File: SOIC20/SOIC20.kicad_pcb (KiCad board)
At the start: 2 copper layers, 25.7 x 18 mm, 7 parts, among them J1 Conn_01x10, J2 Conn_02x10_Counter_Clockwise, J4 Conn_02x10_Counter_Clockwise, J5 Conn_01x10

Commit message: Board Updates
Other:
- board size 25.7 x 18 mm -> 25.4 x 17.8 mm
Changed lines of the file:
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@@
       (xy -0.06096 3.169456) (xy -0.06096 2.6924) (xy 0.07112 2.6924) (xy 0.07112 2.926926)) (layer F.SilkS) (width 0.01))
   )
+  (gr_line (start 77.089 43.7896) (end 77.089 28.5496) (layer Edge.Cuts) (width 0.05))
+  (gr_line (start 52.959 45.0596) (end 75.819 45.0596) (layer Edge.Cuts) (width 0.05))
+  (gr_line (start 51.689 28.5496) (end 51.689 43.7896) (layer Edge.Cuts) (width 0.05))
+  (gr_line (start 75.819 27.2796) (end 52.959 27.2796) (layer Edge.Cuts) (width 0.05))
+  (gr_arc (start 75.819 28.5496) (end 77.089 28.5496) (angle -90) (layer Edge.Cuts) (width 0.05))
+  (gr_arc (start 75.819 43.7896) (end 75.819 45.0596) (angle -90) (layer Edge.Cuts) (width 0.05))
+  (gr_arc (start 52.959 43.7896) (end 51.689 43.7896) (angle -90) (layer Edge.Cuts) (width 0.05))
+  (gr_arc (start 52.959 28.5496) (end 52.959 27.2796) (angle -90) (layer Edge.Cuts) (width 0.05))
   (dimension 18.034 (width 0.15) (layer Dwgs.User)
     (gr_text "18.034 mm" (at 83.215 36.1696 90) (layer Dwgs.User)
@@
     (effects (font (size 0.8 0.7) (thickness 0.13)))
   )
-  (gr_line (start 77.216 43.7896) (end 77.216 28.5496) (layer Edge.Cuts) (width 0.05))
-  (gr_line (start 52.959 45.1866) (end 75.819 45.1866) (layer Edge.Cuts) (width 0.05))
-  (gr_line (start 51.562 28.5496) (end 51.562 43.7896) (layer Edge.Cuts) (width 0.05))
-  (gr_line (start 75.945478 27.158337) (end 52.959 27.1526) (layer Edge.Cuts) (width 0.05))
-  (gr_arc (start 75.819 28.5496) (end 77.216 28.5496) (angle -84.80557109) (layer Edge.Cuts) (width 0.05))
-  (gr_arc (start 75.819 43.7896) (end 75.819 45.1866) (angle -90) (layer Edge.Cuts) (width 0.05))
-  (gr_arc (start 52.959 43.7896) (end 51.562 43.7896) (angle -90) (layer Edge.Cuts) (width 0.05))
-  (gr_arc (start 52.959 28.5496) (end 52.959 27.1526) (angle -90) (layer Edge.Cuts) (width 0.05))
   (segment (start 72.8744 40.845) (end 75.819 43.7896) (width 0.25) (layer F.Cu) (net 1))
   (segment (start 70.0786 40.845) (end 72.8744 40.845) (width 0.25) (layer F.Cu) (net 1))

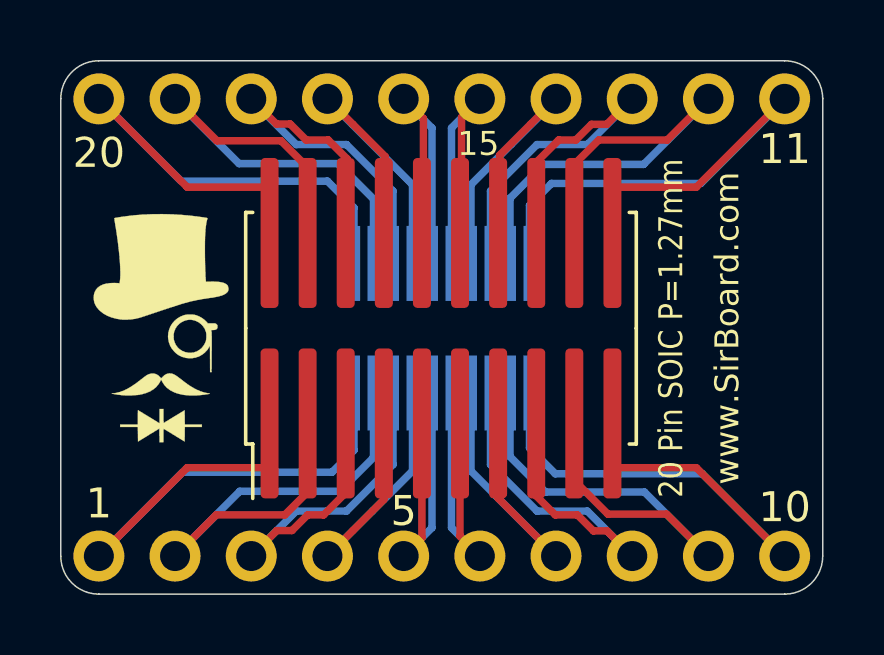
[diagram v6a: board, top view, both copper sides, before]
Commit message: Breakout Boards Revision 2
Renders updated, silkscreen text improved, blurry silkscreen items removed/resized.
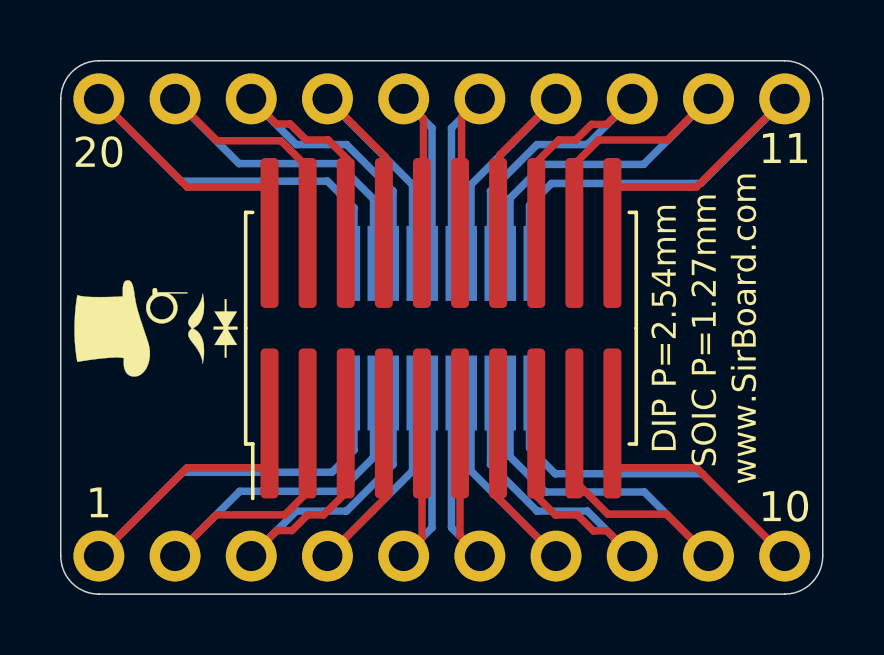
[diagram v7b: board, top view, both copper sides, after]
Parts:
- G***: footprint logo:logo94x134 -> logo:logo76x107
- G***: footprint logo:logo76x107 -> logo:logo54x76
- moved G*** 0.19 mm to (72.5, 36.3), turned to 90 degrees
- moved G*** 0.18 mm to (54.9, 36.2), turned to 90 degrees
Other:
- board text added: "16"
- board text added: "6"
- board text added: "DIP P=2.54mm"
- board text added: "SOIC P=1.27mm"
- board text added: "TSSOP P=0.65mm"
- board text removed: "20 Pin SOIC P=1.27mm"
- board text removed: "20 Pin SSOP P=0.65mm"
